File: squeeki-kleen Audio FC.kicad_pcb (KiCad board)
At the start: 2 copper layers, 50.8 x 15.2 mm, 18 parts, among them J1 GND, J2 VCC, J3 P1, J4 P2, J5 C8, J6 GND out, U1 OPA1671IDCKT

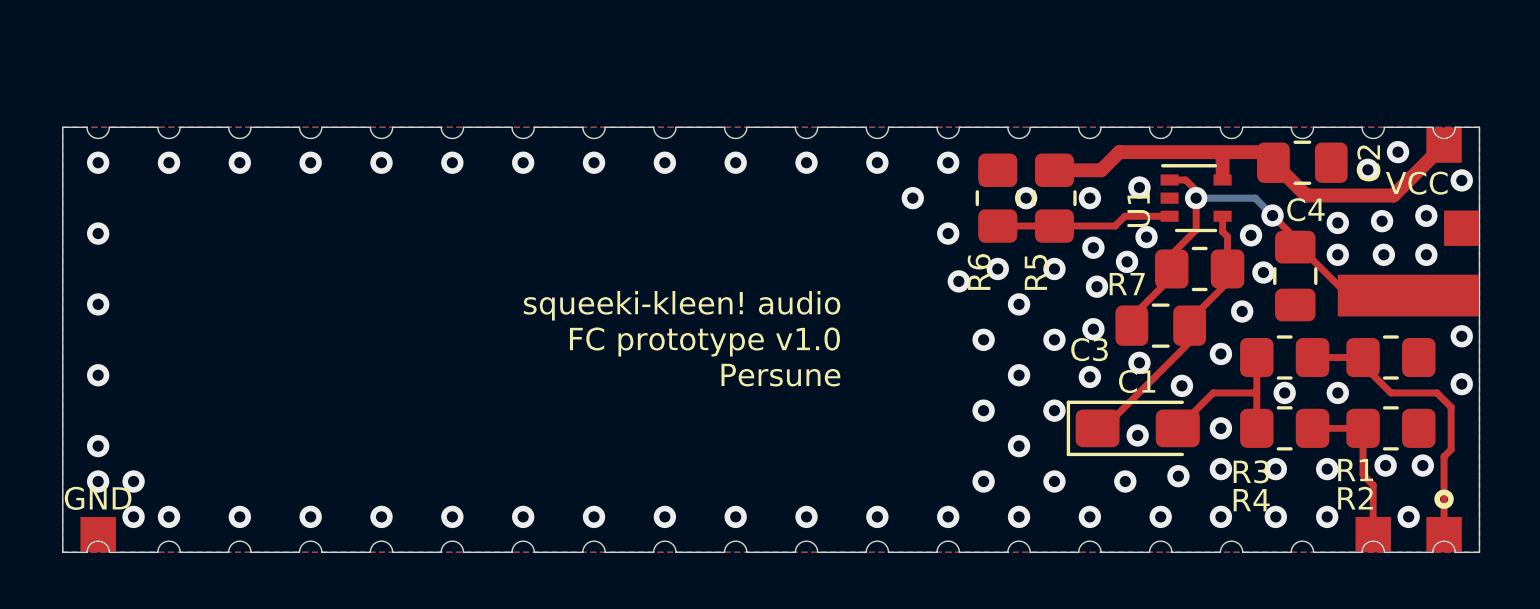
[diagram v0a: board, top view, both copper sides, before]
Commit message: Add readme and license
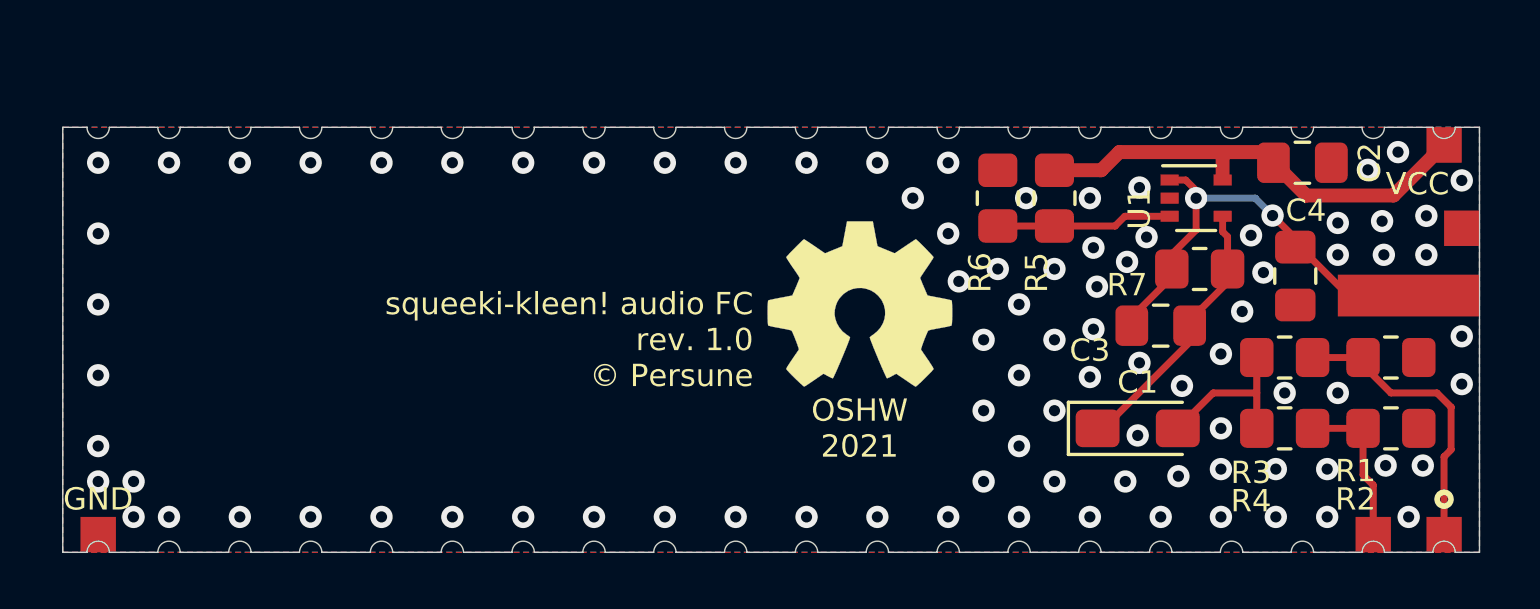
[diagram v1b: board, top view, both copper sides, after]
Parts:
- added REF**: OSHW-Symbol_6.7x6mm_SilkScreen, Symbol:OSHW-Symbol_6.7x6mm_SilkScreen, F.Cu at (69.2, 35.6)
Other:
- board text added: "OSHW 2021"
- board text added: "squeeki-kleen! audio FC rev. 1.0 © Persune"
- board text removed: "squeeki-kleen! audio FC prototype v1.0 Persune"

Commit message: Rev. 1.1.0
- change edge cuts to be more panelization-friendly
- use plated through holes instead of castellated holes
- dagga art by https://twitter.com/pickleknotart
- widen ground pad next to the audio out pad
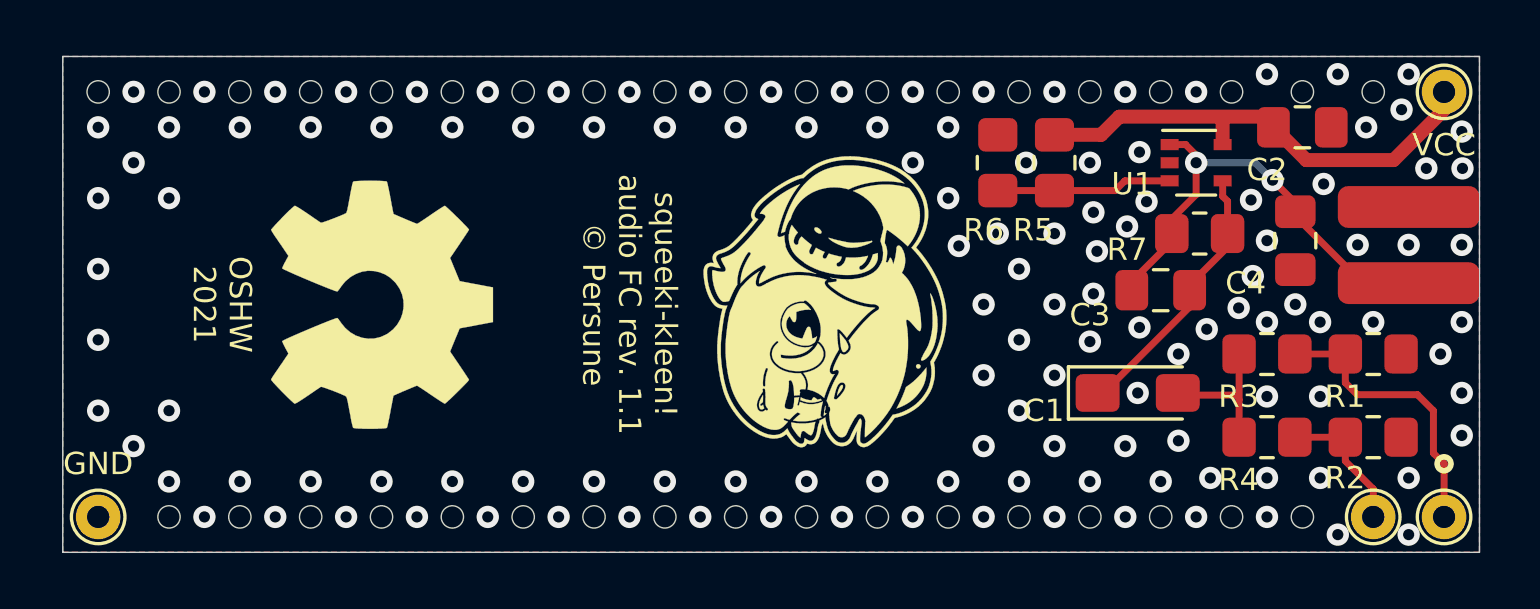
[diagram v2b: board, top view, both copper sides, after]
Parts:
- removed the REF** at (69.2, 35.6)
- added G***: LOGO, custom footprints:dagga, F.Cu at (67.9, 35.6)
- added REF**: OSHW-Symbol_8.9x8mm_SilkScreen, Symbol:OSHW-Symbol_8.9x8mm_SilkScreen, F.Cu at (52.1, 35.6)
- J1, J2, J3, J4: footprint custom footprints:Custom_Pad_Castellated -> custom footprints:Custom_THT
- J6: footprint custom footprints:Custom_Pad_Castellated -> custom footprints:Custom_Pad
- moved J6 2.05 mm to (88.9, 32.1)
- moved J2 1.90 mm to (90.2, 27.9)
- moved C1 1.27 mm to (79.2, 38.7)
- moved C3 1.27 mm to (80.0, 35.1)
- moved C2 1.27 mm to (85.1, 29.2)
- moved R5 1.27 mm to (76.2, 30.5)
- moved R6 1.27 mm to (74.2, 30.5)
- moved U1 1.27 mm to (81.3, 30.5)
- moved C4 1.27 mm to (84.8, 33.3)
- moved R7 1.27 mm to (81.4, 33.0)
- moved R2 0.71 mm to (87.6, 40.3)
- moved R4 0.71 mm to (83.8, 40.3)
- moved R1 0.65 mm to (87.6, 37.3)
- moved R3 0.65 mm to (83.8, 37.3)
- moved J1 0.63 mm to (41.9, 43.2)
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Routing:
- net VCC: track 16.6 -> 17.6 mm
- net Net-(C1-Pad2): track 5.91 -> 5.18 mm
- net /P2: track 5.64 -> 5.08 mm
- net GND: vias 90 -> 129
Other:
- board size 50.8 x 15.2 mm -> 50.8 x 17.8 mm
- board text added: "squeeki-kleen! audio FC rev. 1.1 © Persune"
- board text removed: "squeeki-kleen! audio FC rev. 1.0 © Persune"

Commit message: Rev 1.2.0
- change edge cuts to reduce unused space
- add THT on pin 30 to add support
- add labels on output pads
- thanks to grievre for feedback
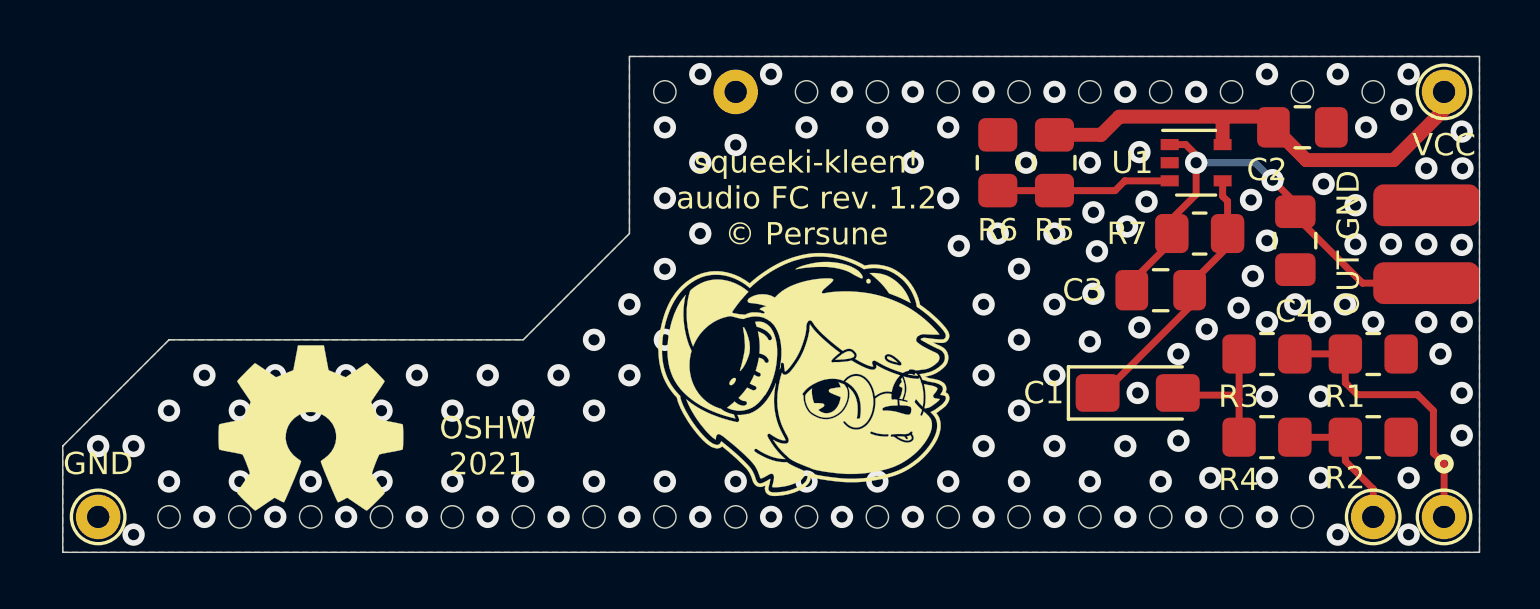
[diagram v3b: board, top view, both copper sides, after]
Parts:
- removed the REF** at (52.1, 35.6)
- added REF**: OSHW-Symbol_6.7x6mm_SilkScreen, Symbol:OSHW-Symbol_6.7x6mm_SilkScreen, F.Cu at (49.5, 40.0)
- added REF**: , TestPoint:TestPoint_THTPad_D1.5mm_Drill0.7mm, B.Cu at (64.8, 27.9)
- moved G*** 2.62 mm to (67.3, 38.1), turned to 0 degrees
- moved J6 0.64 mm to (89.5, 32.0), turned to 90 degrees
- moved J5 0.63 mm to (89.5, 34.8), turned to 90 degrees
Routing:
- net GND: vias 129 -> 134
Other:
- outline, holes or cut-outs redrawn
- board text added: "GND"
- board text added: "OUT"
- board text added: "squeeki-kleen! audio FC rev. 1.2 © Persune"
- board text removed: "squeeki-kleen! audio FC rev. 1.1 © Persune"

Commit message: KiCad 6.0
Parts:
- removed the REF** at (49.5, 40.0)
- added REF**: OSHW-Logo2_7.3x6mm_SilkScreen, Symbol:OSHW-Logo2_7.3x6mm_SilkScreen, F.Cu at (48.3, 40.0)
- R7: value 100K -> 80K
- moved G*** 0.63 mm to (67.3, 37.5)
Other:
- net class Default removed
- net class Power removed
- rule pad_to_mask_clearance: 0.05 -> 0
- board text added: "squeeki-kleen! audio FC r.1.2.1"
- board text added: "© Persune 2021-2022"
- board text removed: "OSHW 2021"
- board text removed: "squeeki-kleen! audio FC rev. 1.2 © Persune"

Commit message: Adjust via size and copper fill
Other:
- board text added: "squeeki-kleen! audio FC r.1.3.0"
- board text removed: "squeeki-kleen! audio FC r.1.2.1"

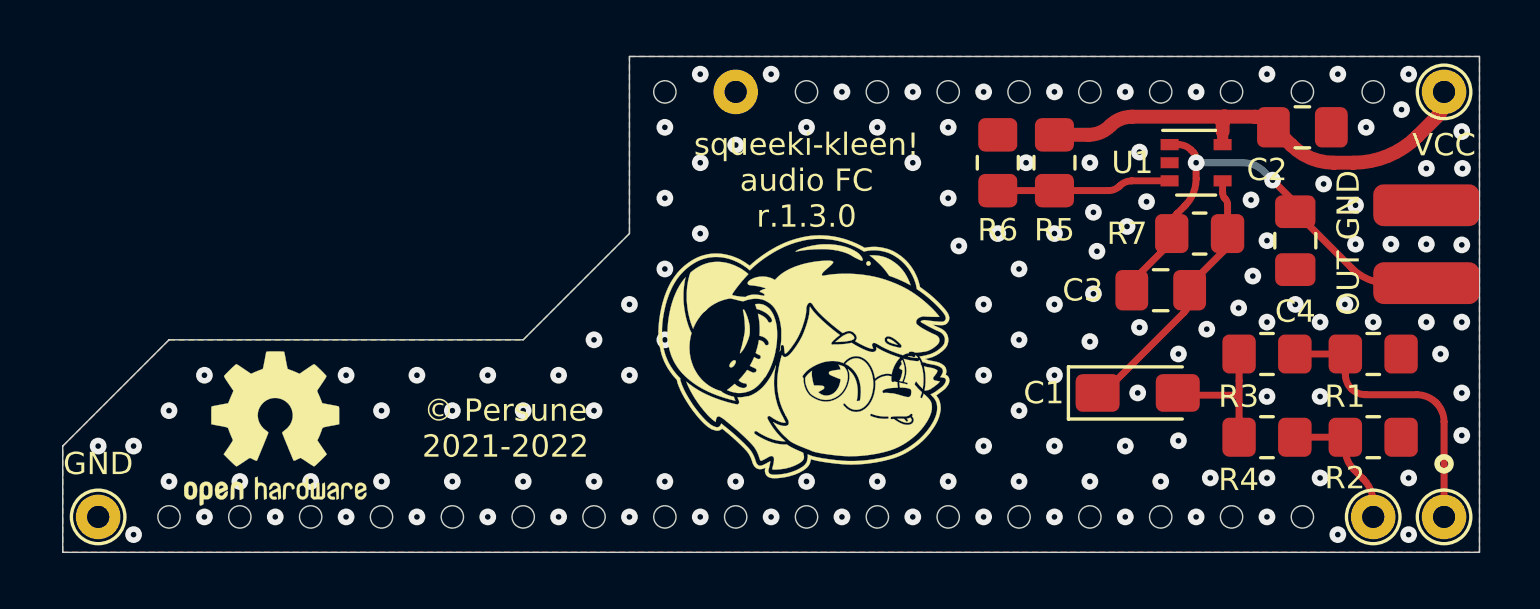
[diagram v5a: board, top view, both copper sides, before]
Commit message: Add teardrops, HTML BOM, and trace rounding
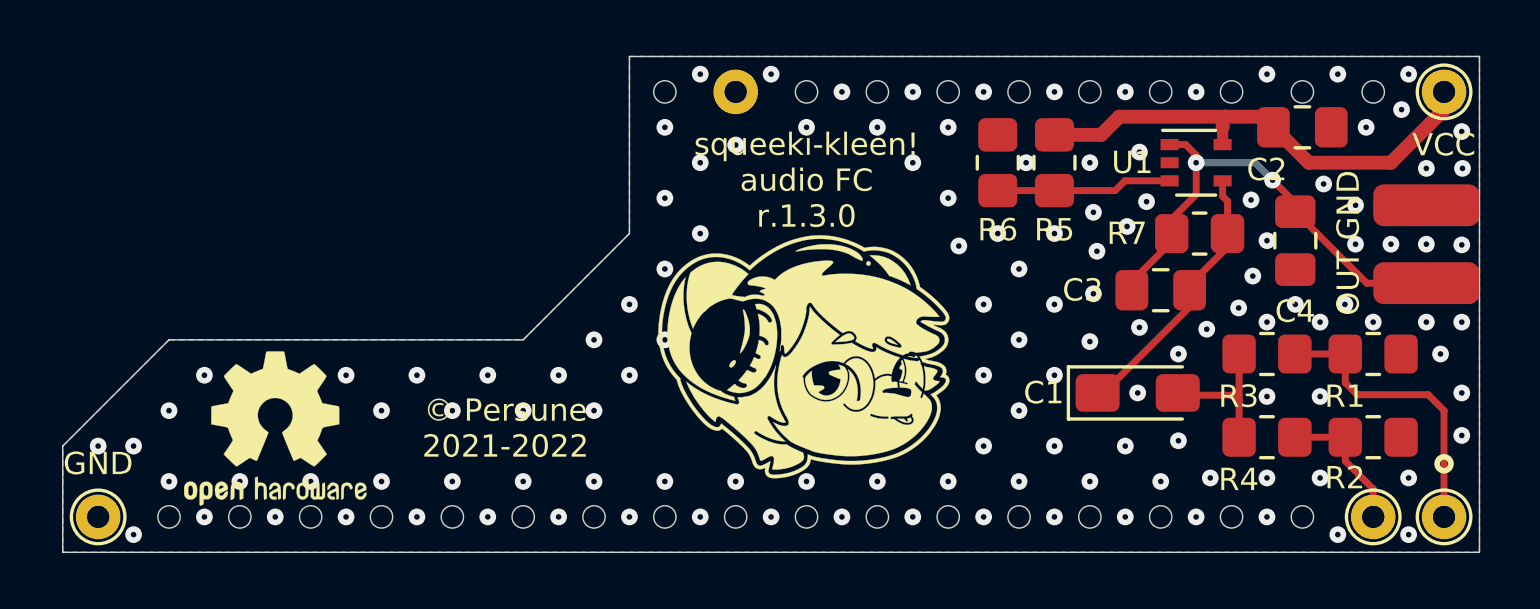
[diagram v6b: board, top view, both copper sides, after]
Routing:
- net VCC: track 17.2 -> 17.8 mm
